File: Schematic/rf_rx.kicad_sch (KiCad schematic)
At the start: 12 parts, among them SW2 TS24CA, U1 ME6217C33M5G, U12 ESP-01F-2M, U13 E28-2G4M27SX

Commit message: Refactor code structure for improved readability and maintainability
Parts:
- removed SW2: TS24CA, fch7_fp:SW-SMD_2P-TS24CA, symbol fch7_sym:TS24CA
- removed U1: ME6217C33M5G, fch7_fp:SOT23-5, symbol ME6217C33M5G:ME6217C33M5G
- added SW2: TS24CA, fch7_fp:SW-SMD_2P-TS24CA, symbol fclib:TS24CA
- added U1: ME6217C33M5G, fch7_fp:SOT23-5, symbol fclib:ME6217C33M5G
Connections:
- net 4V5: now also U1.1 (IN), U1.3 (CE)
- net GND: now also SW2.2, U1.2 (GND)
- net VDD_RECV: now also U1.5 (OUT)
- net at U13.17 (IO0): now also SW2.1
- new net: SW2.3, SW2.4

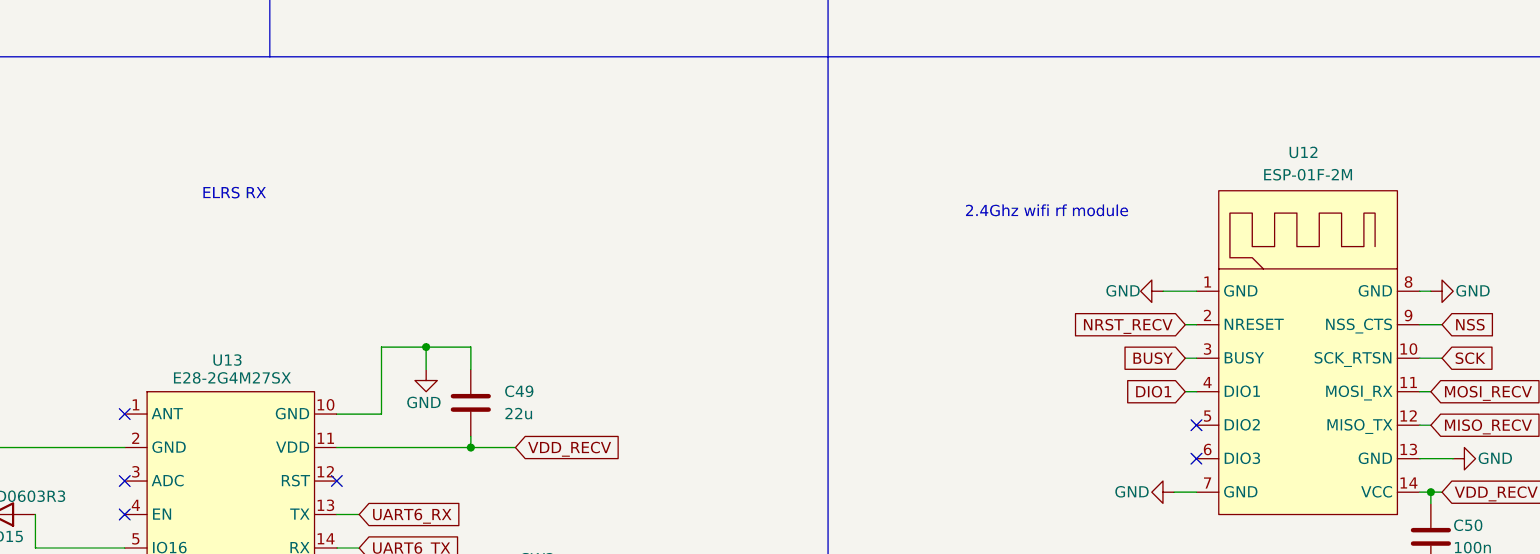
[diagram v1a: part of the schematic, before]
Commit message: Update component properties for RF receiver schematic
- Changed the "Value" and "MPN" properties of components in the rf_rx.kicad_sch file from "E28-2G4M27SX" to "ESP-01F-2M".
- Reversed the previous changes for the same properties, updating them back to "E28-2G4M27SX".
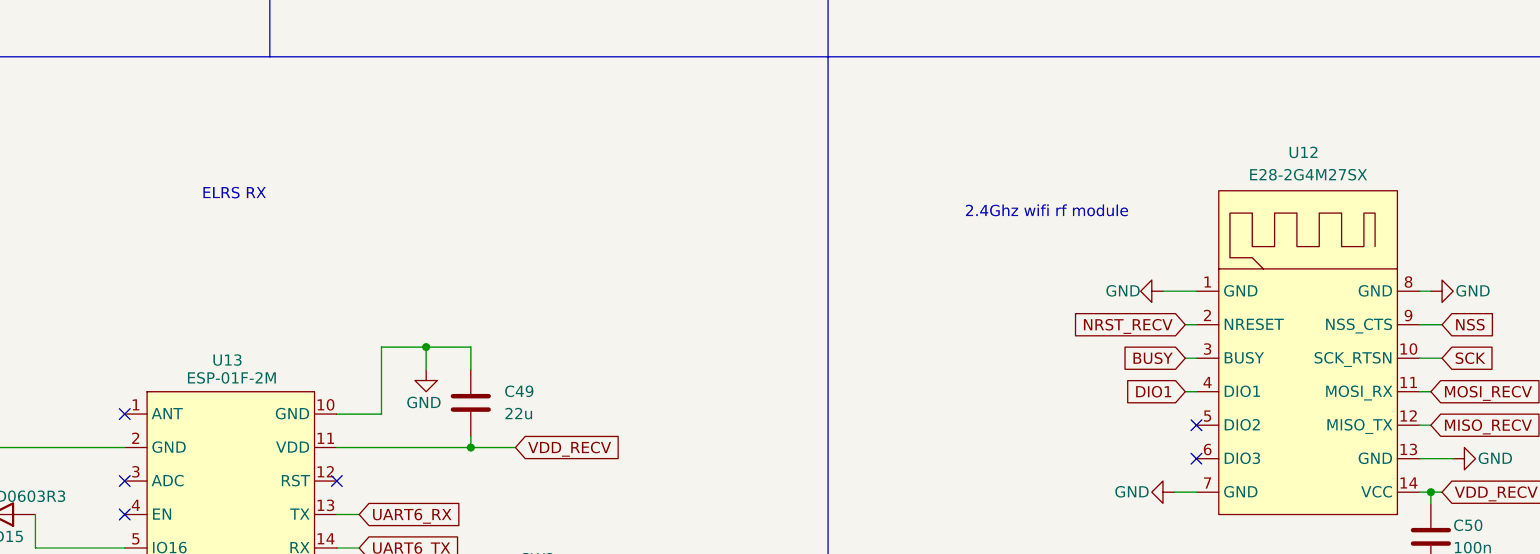
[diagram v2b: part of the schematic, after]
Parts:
- U12: value ESP-01F-2M -> E28-2G4M27SX; MPN ESP-01F-2M -> E28-2G4M27SX
- U13: value E28-2G4M27SX -> ESP-01F-2M; MPN E28-2G4M27SX -> ESP-01F-2M
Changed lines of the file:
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@@
 			)
 		)
-		(property "Value" "E28-2G4M27SX"
+		(property "Value" "ESP-01F-2M"
 			(at 76.962 121.666 0)
 			(effects
@@
 			)
 		)
-		(property "MPN" "E28-2G4M27SX"
+		(property "MPN" "ESP-01F-2M"
 			(at 91.694 116.586 0)
 			(effects
@@
 			)
 		)
-		(property "Value" "ESP-01F-2M"
+		(property "Value" "E28-2G4M27SX"
 			(at 199.39 98.552 0)
 			(effects
@@
 			)
 		)
-		(property "MPN" "ESP-01F-2M"
+		(property "MPN" "E28-2G4M27SX"
 			(at 229.108 116.332 0)
 			(effects

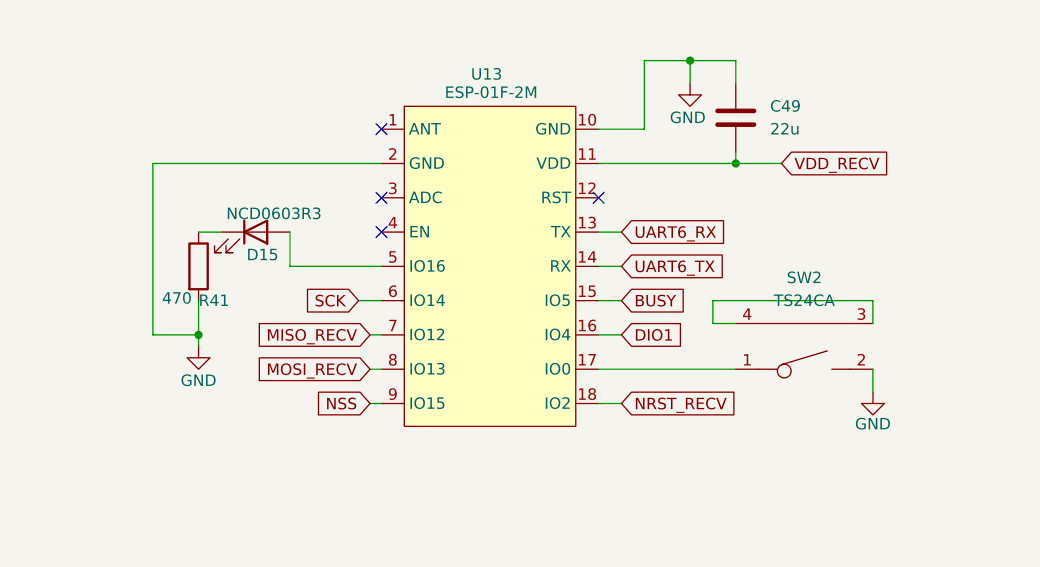
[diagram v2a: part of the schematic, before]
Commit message: Refactor schematic files and add net definitions
- Updated priority values for GND and POWER net classes in fch7.kicad_pro.
- Added USB_DIFF net class with associated patterns for USB differential signals.
- Removed duplicate junctions and adjusted wire connections in rf_rx.kicad_sch for clarity.
- Adjusted component positions and properties in rf_rx.kicad_sch for better layout.
- Modified text positions for IMU components in sensors.kicad_sch to improve readability.
- Cleaned up unnecessary wires and added new connections in sensors.kicad_sch.
- Introduced nets.txt file to define various electrical nets used across the schematics.
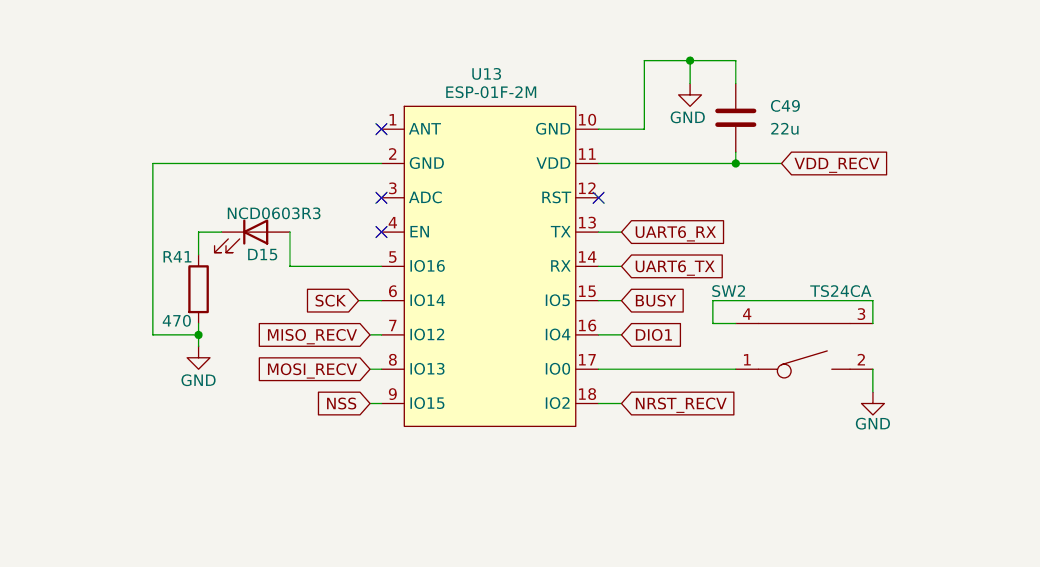
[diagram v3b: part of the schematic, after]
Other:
- moved on the sheet: R41
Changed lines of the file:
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@@
+	)
+	(junction
+		(at 111.76 39.37)
+		(diameter 0)
+		(color 0 0 0 0)
+	)
+	(junction
+		(at 104.14 129.54)
+		(diameter 0)
+		(color 0 0 0 0)
+	)
+	(junction
+		(at 99.06 118.11)
+		(diameter 0)
+		(color 0 0 0 0)
 	)
 	(junction
@@
 	)
 	(junction
-		(at 111.76 39.37)
-		(diameter 0)
-		(color 0 0 0 0)
-	)
-	(junction
-		(at 104.14 129.54)
-		(diameter 0)
-		(color 0 0 0 0)
-	)
-	(junction
-		(at 99.06 118.11)
-		(diameter 0)
-		(color 0 0 0 0)
-	)
-	(junction
 		(at 213.36 134.62)
 		(diameter 0)
@@
 	(wire
 		(pts
+			(xy 44.45 147.32) (xy 44.45 148.59)
+		)
+		(stroke
+			(width 0)
+			(type default)
+		)
+	)
+	(wire
+		(pts
 			(xy 99.06 49.53) (xy 99.06 55.88)
 		)
@@
 	(wire
 		(pts
-			(xy 44.45 137.16) (xy 46.99 137.16)
-		)
-		(stroke
-			(width 0)
-			(type default)
-		)
-	)
-	(wire
-		(pts
 			(xy 88.9 125.73) (xy 93.98 125.73)
 		)
@@
 	(wire
 		(pts
+			(xy 46.99 137.16) (xy 44.45 137.16)
+		)
+		(stroke
+			(width 0)
+			(type default)
+		)
+	)
+	(wire
+		(pts
 			(xy 104.14 147.32) (xy 101.6 147.32)
 		)
@@
 	(wire
 		(pts
-			(xy 44.45 144.78) (xy 44.45 148.59)
-		)
-		(stroke
-			(width 0)
-			(type default)
-		)
-	)
-	(wire
-		(pts
 			(xy 125.73 46.99) (xy 125.73 48.26)
 		)
@@
 		(pts
 			(xy 213.36 134.62) (xy 213.36 135.89)
+		)
+		(stroke
+			(width 0)
+			(type default)
+		)
+	)
+	(wire
+		(pts
+			(xy 44.45 137.16) (xy 44.45 139.7)
 		)
 		(stroke
@@
 	(symbol
 		(lib_id "Device:R")
-		(at 44.45 140.97 0)
+		(at 44.45 143.51 0)
 		(unit 1)
 		(exclude_from_sim no)
@@
 		(dnp no)
 		(property "Reference" "R41"
-			(at 44.45 144.78 0)
+			(at 40.386 139.954 0)
 			(effects
 				(font
@@
 		)
 		(property "Value" "470"
-			(at 40.386 144.526 0)
+			(at 40.386 147.066 0)
 			(effects
 				(font
@@
 		)
 		(property "Footprint" "Resistor_SMD:R_0603_1608Metric"
-			(at 42.672 140.97 90)
+			(at 42.672 143.51 90)
 			(effects
 				(font
@@
 		)
 		(property "Datasheet" "https://www.lcsc.com/datasheet/C23179.pdf"
-			(at 44.45 140.97 0)
+			(at 44.45 143.51 0)
 			(effects
 				(font
@@
 		)
 		(property "Description" "Resistor"
-			(at 44.45 140.97 0)
+			(at 44.45 143.51 0)
 			(effects
 				(font
@@
 		)
 		(property "Fréquence" ""
-			(at 44.45 140.97 0)
+			(at 44.45 143.51 0)
 			(effects
 				(font
@@
 		)
 		(property "MPN" "0603WAF4700T5E"
-			(at 44.45 140.97 0)
+			(at 44.45 143.51 0)
 			(effects
 				(font
@@
 		)
 		(property "Manufacturer" "UNI-ROYAL"
-			(at 44.45 140.97 0)
+			(at 44.45 143.51 0)
 			(effects
 				(font
@@
 		(on_board yes)
 		(dnp no)
-		(fields_autoplaced yes)
 		(property "Reference" "SW2"
-			(at 111.76 142.24 0)
+			(at 103.378 143.764 0)
 			(effects
 				(font
@@
 		)
 		(property "Value" "TS24CA"
-			(at 111.76 144.78 0)
+			(at 115.824 143.764 0)
 			(effects
 				(font
@@
 		(on_board yes)
 		(dnp no)
-		(fields_autoplaced yes)
 		(property "Reference" "U1"
 			(at 44.45 49.53 0)

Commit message: Refactor code structure and remove redundant sections for improved readability
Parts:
- removed C49: 22u, Capacitor_SMD:C_0805_2012Metric, symbol Device:C
- removed D15: NCD0603R3, fch7_fp:LED0603-R-RD_RED, symbol Device:LED
- removed R41: 470, Resistor_SMD:R_0603_1608Metric, symbol Device:R
- removed SW2: TS24CA, fch7_fp:SW-SMD_2P-TS24CA, symbol fclib:TS24CA
- removed U13: ESP-01F-2M, fch7_fp:WIFIM-SMD_ESP-01F-2M, symbol fclib:elrs_rx
- added R23: 10k, Resistor_SMD:R_0603_1608Metric, symbol Device:R
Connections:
- net MISO_RECV is gone; now on net UART6_RX: U12.12 (MISO_TX)
- net MOSI_RECV is gone; now on net UART6_TX: U12.11 (MOSI_RX)
- net NRST_RECV is gone; now on net GND: U12.2 (NRESET)
- net GND: now also R23.2
- net VDD_RECV: now also R23.1
- net BUSY: no longer names the net of U12.3 (BUSY)
- net DIO1: no longer names the net of U12.4 (DIO1)
- net NSS: no longer names the net of U12.9 (NSS_CTS)
- net SCK: no longer names the net of U12.10 (SCK_RTSN)
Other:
- note removed: "2.4Ghz wifi rf module"
- moved on the sheet: C50, U12

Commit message: Re-introduced MPU6500, every component in place with their 3d model, every track is routed
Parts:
- D14: footprint fch7_fp:LED0603-R-RD_RED -> LED_SMD:LED_0603_1608Metric
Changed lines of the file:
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@@
 			)
 		)
-		(property "Footprint" "fch7_fp:LED0603-R-RD_RED"
+		(property "Footprint" "LED_SMD:LED_0603_1608Metric"
 			(at 125.73 43.18 0)
 			(effects

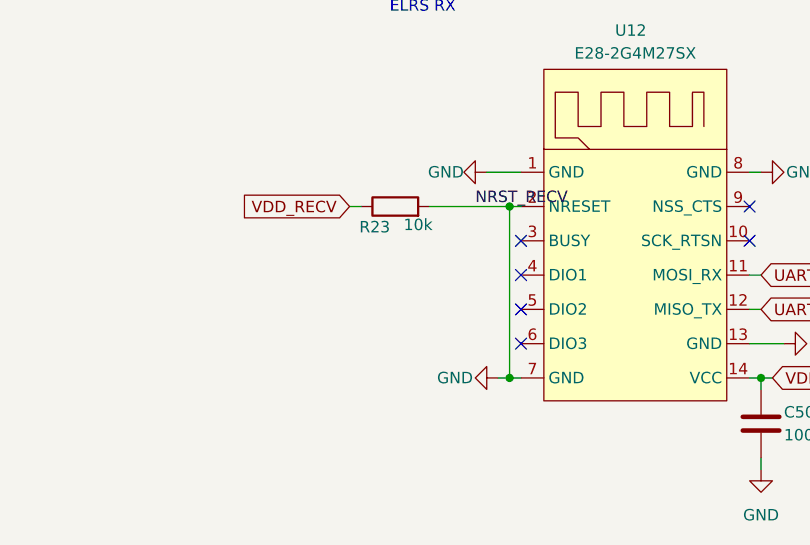
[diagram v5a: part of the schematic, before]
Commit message: finished every routing and fix errors in DRC
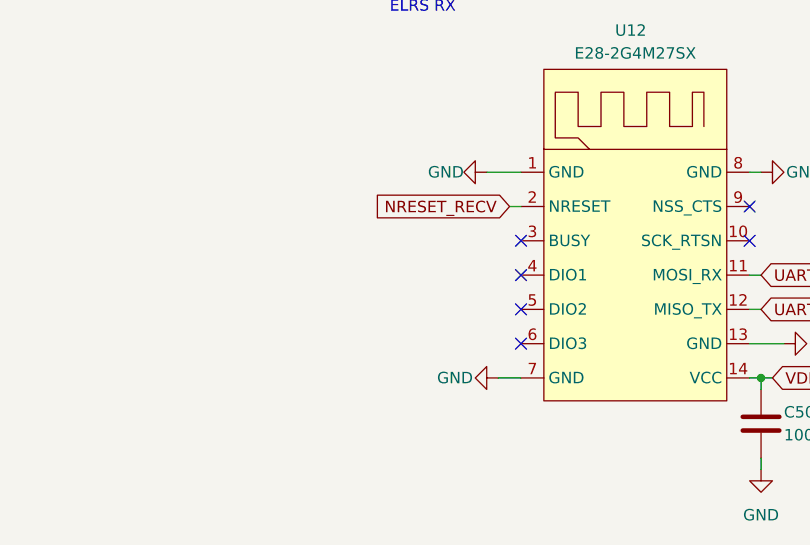
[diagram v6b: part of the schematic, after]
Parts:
- removed R23: 10k, Resistor_SMD:R_0603_1608Metric, symbol Device:R
- U1: footprint fch7_fp:SOT23-5 -> fch7:SOT23-5
- U12: footprint fch7_fp:WIRELM-SMD_E28-2G4M27SX -> fch7:WIRELM-SMD_E28-2G4M27SX
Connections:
- net GND: no longer U12.2 (NRESET)
- new net NRESET_RECV: U12.2 (NRESET)
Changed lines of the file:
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@@
-	)
-	(junction
-		(at 66.04 149.86)
-		(diameter 0)
-		(color 0 0 0 0)
 	)
 	(junction
@@
 	)
 	(junction
-		(at 66.04 130.81)
-		(diameter 0)
-		(color 0 0 0 0)
-	)
-	(junction
 		(at 93.98 149.86)
 		(diameter 0)
@@
 	(wire
 		(pts
+			(xy 66.04 130.81) (xy 67.31 130.81)
+		)
+		(stroke
+			(width 0)
+			(type default)
+		)
+	)
+	(wire
+		(pts
 			(xy 31.75 57.15) (xy 30.48 57.15)
 		)
@@
 		)
 	)
-	(wire
-		(pts
-			(xy 57.15 130.81) (xy 66.04 130.81)
-		)
-		(stroke
-			(width 0)
-			(type default)
-		)
-	)
-	(wire
-		(pts
-			(xy 48.26 130.81) (xy 49.53 130.81)
-		)
-		(stroke
-			(width 0)
-			(type default)
-		)
-	)
 	(polyline
 		(pts
@@
 	(wire
 		(pts
-			(xy 66.04 130.81) (xy 66.04 149.86)
-		)
-		(stroke
-			(width 0)
-			(type default)
-		)
-	)
-	(wire
-		(pts
 			(xy 113.03 35.56) (xy 111.76 35.56)
 		)
@@
 	(wire
 		(pts
-			(xy 66.04 130.81) (xy 67.31 130.81)
-		)
-		(stroke
-			(width 0)
-			(type default)
-		)
-	)
-	(wire
-		(pts
 			(xy 111.76 41.91) (xy 111.76 39.37)
 		)
@@
 	(wire
 		(pts
-			(xy 64.77 149.86) (xy 66.04 149.86)
+			(xy 64.77 149.86) (xy 67.31 149.86)
 		)
 		(stroke
@@
 	(wire
 		(pts
-			(xy 66.04 149.86) (xy 67.31 149.86)
-		)
-		(stroke
-			(width 0)
-			(type default)
-		)
-	)
-	(wire
-		(pts
 			(xy 92.71 142.24) (xy 93.98 142.24)
 		)
@@
 			(width 0)
 			(type default)
-		)
-	)
-	(label "NRST_RECV"
-		(at 62.23 130.81 0)
-		(effects
-			(font
-				(size 1.27 1.27)
-			)
-			(justify bottom)
 		)
 	)
@@
 		)
 	)
-	(global_label "VDD_RECV"
+	(global_label "NRESET_RECV"
 		(shape input)
-		(at 48.26 130.81 180)
+		(at 66.04 130.81 180)
 		(fields_autoplaced yes)
 		(effects
@@
 		)
 		(property "Intersheetrefs" "${INTERSHEET_REFS}"
-			(at 35.901 130.81 0)
+			(at 50.234 130.81 0)
 			(effects
 				(font
@@
 	)
 	(symbol
-		(lib_id "Device:R")
-		(at 53.34 130.81 90)
-		(unit 1)
-		(exclude_from_sim no)
-		(in_bom yes)
-		(on_board yes)
-		(dnp no)
-		(property "Reference" "R23"
-			(at 51.054 133.096 90)
-			(effects
-				(font
-					(size 1.27 1.27)
-				)
-			)
-		)
-		(property "Value" "10k"
-			(at 55.88 132.842 90)
-			(effects
-				(font
-					(size 1.27 1.27)
-				)
-			)
-		)
-		(property "Footprint" "Resistor_SMD:R_0603_1608Metric"
-			(at 53.34 132.588 90)
-			(effects
-				(font
-					(size 1.27 1.27)
-				)
-				(hide yes)
-			)
-		)
-		(property "Datasheet" "https://www.lcsc.com/datasheet/C23179.pdf"
-			(at 53.34 130.81 0)
-			(effects
-				(font
-					(size 1.27 1.27)
-				)
-				(hide yes)
-			)
-		)
-		(property "Description" "Resistor"
-			(at 53.34 130.81 0)
-			(effects
-				(font
-					(size 1.27 1.27)
-				)
-				(hide yes)
-			)
-		)
-		(property "Fréquence" ""
-			(at 53.34 130.81 0)
-			(effects
-				(font
-					(size 1.27 1.27)
-				)
-				(hide yes)
-			)
-		)
-		(property "MPN" "0603WAF4700T5E"
-			(at 53.34 130.81 0)
-			(effects
-				(font
-					(size 1.27 1.27)
-				)
-				(hide yes)
-			)
-		)
-		(property "Manufacturer" "UNI-ROYAL"
-			(at 53.34 130.81 0)
-			(effects
-				(font
-					(size 1.27 1.27)
-				)
-				(hide yes)
-			)
-		)
-		(pin "1"
-		)
-		(pin "2"
-		)
-		(instances
-			(project "fch7"
-				(path "/11716af6-0e6e-444b-b738-3f12da23c1a2/c005db94-b190-4389-8874-35307c577c05"
-					(reference "R23")
-					(unit 1)
-				)
-			)
-		)
-	)
-	(symbol
 		(lib_id "power:GND")
 		(at 111.76 57.15 0)
@@
 			)
 		)
-		(property "Footprint" "fch7_fp:SOT23-5"
+		(property "Footprint" "fch7:SOT23-5"
 			(at 44.45 59.69 0)
 			(effects
@@
 			)
 		)
-		(property "Footprint" "fch7_fp:WIRELM-SMD_E28-2G4M27SX"
+		(property "Footprint" "fch7:WIRELM-SMD_E28-2G4M27SX"
 			(at 80.01 134.62 0)
 			(effects

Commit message: update schematic after reviewing some footprints
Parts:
- C47, C50: MPN 0603B104K500NT -> (none); Manufacturer FH -> (none)
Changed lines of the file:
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@@
 			)
 		)
-		(property "Datasheet" "https://www.lcsc.com/datasheet/C30926.pdf"
+		(property "Datasheet" ""
 			(at 93.98 154.94 0)
 			(effects
@@
 			)
 		)
-		(property "MPN" "0603B104K500NT "
+		(property "MPN" ""
 			(at 93.98 154.94 0)
 			(effects
@@
 			)
 		)
-		(property "Manufacturer" "FH"
+		(property "Manufacturer" ""
 			(at 93.98 154.94 0)
 			(effects
@@
 			)
 		)
-		(property "Datasheet" "https://www.lcsc.com/datasheet/C30926.pdf"
+		(property "Datasheet" ""
 			(at 99.06 45.72 0)
 			(effects
@@
 			)
 		)
-		(property "MPN" "0603B104K500NT "
+		(property "MPN" ""
 			(at 99.06 45.72 0)
 			(effects
@@
 			)
 		)
-		(property "Manufacturer" "FH"
+		(property "Manufacturer" ""
 			(at 99.06 45.72 0)
 			(effects
